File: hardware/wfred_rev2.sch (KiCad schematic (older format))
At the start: 8 parts, among them U101 L6920D

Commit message: Added Reichelt/Mouser part numbers for all parts except ESP12-E/F
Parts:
- B101: Reichelt (none) -> KEYSTONE 1013
- L101: Reichelt L-PISM 22µ -> L-242418FPS 22µ
- U101: Mouser (none) -> 511-L6920DTR
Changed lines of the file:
@@
 F 2 "myFootprints:L_2424_HandSoldering" H 4300 1400 60  0001 C CNN
 F 3 "" H 4300 1400 60  0000 C CNN
-F 4 "L-PISM 22µ" V 4300 1400 60  0001 C CNN "Reichelt"
+F 4 "L-242418FPS 22µ" V 4300 1400 60  0001 C CNN "Reichelt"
 	1    4300 1400
 	1    0    0    -1
@@
 F 3 "" H 4300 2500 60  0001 C CNN
 F 4 "L 6920 D" H 4300 2500 60  0001 C CNN "Reichelt"
+F 5 "511-L6920DTR" H 4300 2500 60  0001 C CNN "Mouser"
 	1    4300 2500
 	1    0    0    -1
@@
 F 2 "myFootprints:KEYSTONE1013" H 1200 4900 60  0001 C CNN
 F 3 "" H 1200 4900 60  0001 C CNN
+F 4 "KEYSTONE 1013" H 1200 4900 60  0001 C CNN "Reichelt"
 	1    1200 4900
 	0    1    1    0

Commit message: Created new 3D renderings
- In the process, kicad "rescued" some symbols
- Also added the value to the crystal in the schematic
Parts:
- C101, C102, C103, C104, C105: symbol C -> C-RESCUE-wfred_rev2
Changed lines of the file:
@@
 EESchema Schematic File Version 2
+LIBS:wfred_rev2-rescue
 LIBS:power
 LIBS:device
@@
 Connection ~ 5500 2200
 $Comp
-L C C101
+L C-RESCUE-wfred_rev2 C101
 U 1 1 5920B38E
 P 2150 2900
@@
 $EndComp
 $Comp
-L GND #PWR01
+L GND-RESCUE-wfred_rev2 #PWR01
 U 1 1 5920B390
 P 2150 3300
@@
 $EndComp
 $Comp
-L GND #PWR02
+L GND-RESCUE-wfred_rev2 #PWR02
 U 1 1 5920B391
 P 1850 3300
@@
 $EndComp
 $Comp
-L GND #PWR03
+L GND-RESCUE-wfred_rev2 #PWR03
 U 1 1 5920B392
 P 2450 3300
@@
 NoConn ~ 3600 2200
 $Comp
-L C C103
+L C-RESCUE-wfred_rev2 C103
 U 1 1 5920B397
 P 3300 2900
@@
 $EndComp
 $Comp
-L GND #PWR06
+L GND-RESCUE-wfred_rev2 #PWR06
 U 1 1 5920B398
 P 3300 3300
@@
 $EndComp
 $Comp
-L GND #PWR07
+L GND-RESCUE-wfred_rev2 #PWR07
 U 1 1 5920B399
 P 3500 3300
@@
 $EndComp
 $Comp
-L GND #PWR09
+L GND-RESCUE-wfred_rev2 #PWR09
 U 1 1 5920B39D
 P 6300 3300
@@
 $EndComp
 $Comp
-L GND #PWR010
+L GND-RESCUE-wfred_rev2 #PWR010
 U 1 1 5920B39E
 P 6600 3300
@@
 $EndSheet
 $Comp
-L C C102
+L C-RESCUE-wfred_rev2 C102
 U 1 1 59210DD0
 P 2450 2900
@@
 $EndComp
 $Comp
-L C C104
+L C-RESCUE-wfred_rev2 C104
 U 1 1 59210E13
 P 6300 2600
@@
 $EndComp
 $Comp
-L C C105
+L C-RESCUE-wfred_rev2 C105
 U 1 1 59210E8B
 P 6600 2600

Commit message: Switched schematic over to LiPo cell
- Removed AA battery holder
- Removed switching power regulator
- Added micro USB connector
- Added two pin battery connector
- Added LiPo charging IC
- Added 3.0V linear regulator
- Replaced ATMega328 with ATMega32
- Added F5-F8 keys
- Removed SHIFT2 key
- Moved LOCO keys from ESP to ATMega32
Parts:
- removed B101: BATT_HOLDER, myFootprints:KEYSTONE1013, symbol BATT_HOLDER
- removed C101, C102, C104: 22u/25V, Capacitors_SMD:C_0805_HandSoldering, symbol C-RESCUE-wfred_rev2
- removed C103: 100n, Capacitors_SMD:C_0805_HandSoldering, symbol C-RESCUE-wfred_rev2
- removed L101: 22u, myFootprints:L_2424_HandSoldering, symbol INDUCTOR
- removed U101: L6920D, Housings_SSOP:TSSOP-8_4.4x3mm_Pitch0.65mm, symbol L6920D
- added C101, C102: 4u7, symbol C
- added C103: 1u, symbol C
- added CON101: USB-MICRO-B, symbol USB-MINI-B
- added D101: LED - red, symbol LED
- added D102: LED - green, symbol LED
- added IC101: MCP73831T-2ACI_OT, SOT95P270X145-5N, symbol MCP73831T-2ACI_OT
- added IC102: LDL1117S30R, SOT230P700X182-4N, symbol LDL1117S30R
- added P101: BATT, symbol CONN_2
- added R101, R102: 680R, symbol R
- added R103: 2k2, symbol R
- C105: value 22u/25V -> 4u7
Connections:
- net labels added: +5V
- wire segments 26 -> 45
- no-connect marks 2 -> 3
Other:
- moved on the sheet: C105

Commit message: Changed power concept (again)
- Exchanged regulator for one with lower shutdown current
- Moved AVR directly to battery
- Added voltage regulator enable connection to AVR
- Added Speed potentiometer power supply from AVR

New power concept: AVR stays always-on (POWER DOWN MODE if not in use)
and shuts down speed potentiometer and ESP8266 when idle or battery low
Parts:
- removed IC102: LDL1117S30R, SOT230P700X182-4N, symbol LDL1117S30R
- added IC102: NCV8161BSN300T1G, SOT95P275X110-5N, symbol NCV8161BSN300T1G
- C105: value 4u7 -> 1u
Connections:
- net labels added: ESP_ENABLE
- wire segments 45 -> 47
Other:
- moved on the sheet: C105

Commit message: First PCB draft for LiPo version
- Returned to ATMega328 / not enough space for ATMega32
- Moved to multiplexing key and direction inputs -> kept F5-F8
- Most traces are now 0.5mm wide
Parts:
- C101, C102, C103, R101, R102, R103: footprint (none) -> Capacitors_SMD:C_0805_HandSoldering
- CON101: footprint (none) -> Connectors_USB:USB_Micro-B_Molex-105017-0001; Mouser (none) -> 538-105017-0001
- D101, D102: footprint (none) -> myFootprints:LED_D3.0mm
- IC101: footprint SOT95P270X145-5N -> MCP73831T-2ACI_OT:SOT95P270X145-5N
- IC102: footprint SOT95P275X110-5N -> NCV8161BSN300T1G:SOT95P275X110-5N
- P101: footprint (none) -> Pin_Headers:Pin_Header_Angled_1x02_Pitch2.54mm
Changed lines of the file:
@@
 F 0 "P101" V 1350 1600 40  0000 C CNN
 F 1 "BATT" V 1450 1600 40  0000 C CNN
-F 2 "" H 1400 1600 60  0001 C CNN
+F 2 "Pin_Headers:Pin_Header_Angled_1x02_Pitch2.54mm" H 1400 1600 60  0001 C CNN
 F 3 "" H 1400 1600 60  0001 C CNN
 	1    1400 1600
@@
 F 0 "CON101" H 1800 3950 60  0000 C CNN
 F 1 "USB-MICRO-B" H 2000 3000 60  0000 C CNN
-F 2 "" H 2050 3500 60  0001 C CNN
+F 2 "Connectors_USB:USB_Micro-B_Molex-105017-0001" H 2050 3500 60  0001 C CNN
 F 3 "" H 2050 3500 60  0001 C CNN
+F 4 "538-105017-0001" H 2050 3500 60  0001 C CNN "Mouser"
 	1    2050 3500
 	1    0    0    -1
@@
 F 0 "C101" H 4200 3300 40  0000 L CNN
 F 1 "4u7" H 4206 3115 40  0000 L CNN
-F 2 "" H 4238 3050 30  0000 C CNN
+F 2 "Capacitors_SMD:C_0805_HandSoldering" H 4238 3050 30  0001 C CNN
 F 3 "" H 4200 3200 60  0000 C CNN
 	1    4200 3200
@@
 F 0 "R101" V 3780 1550 40  0000 C CNN
 F 1 "680R" V 3707 1551 40  0000 C CNN
-F 2 "" V 3630 1550 30  0000 C CNN
+F 2 "Capacitors_SMD:C_0805_HandSoldering" V 3630 1550 30  0001 C CNN
 F 3 "" H 3700 1550 30  0000 C CNN
 	1    3700 1550
@@
 F 0 "R102" V 3780 3250 40  0000 C CNN
 F 1 "680R" V 3707 3251 40  0000 C CNN
-F 2 "" V 3630 3250 30  0000 C CNN
+F 2 "Capacitors_SMD:C_0805_HandSoldering" V 3630 3250 30  0001 C CNN
 F 3 "" H 3700 3250 30  0000 C CNN
 	1    3700 3250
@@
 F 0 "D101" H 3700 2200 50  0000 C CNN
 F 1 "LED - red" H 3700 2000 50  0000 C CNN
-F 2 "" H 3700 2100 60  0000 C CNN
+F 2 "myFootprints:LED_D3.0mm" H 3700 2100 60  0001 C CNN
 F 3 "" H 3700 2100 60  0000 C CNN
 	1    3700 2100
@@
 F 0 "D102" H 3700 2800 50  0000 C CNN
 F 1 "LED - green" H 3700 2600 50  0000 C CNN
-F 2 "" H 3700 2700 60  0000 C CNN
+F 2 "myFootprints:LED_D3.0mm" H 3700 2700 60  0001 C CNN
 F 3 "" H 3700 2700 60  0000 C CNN
 	1    3700 2700
@@
 F 0 "C102" H 6400 3300 40  0000 L CNN
 F 1 "4u7" H 6406 3115 40  0000 L CNN
-F 2 "" H 6438 3050 30  0000 C CNN
+F 2 "Capacitors_SMD:C_0805_HandSoldering" H 6438 3050 30  0001 C CNN
 F 3 "" H 6400 3200 60  0000 C CNN
 	1    6400 3200
@@
 F 0 "R103" V 6180 3250 40  0000 C CNN
 F 1 "2k2" V 6107 3251 40  0000 C CNN
-F 2 "" V 6030 3250 30  0000 C CNN
+F 2 "Capacitors_SMD:C_0805_HandSoldering" V 6030 3250 30  0001 C CNN
 F 3 "" H 6100 3250 30  0000 C CNN
 	1    6100 3250
@@
 F 0 "C103" H 7500 2600 40  0000 L CNN
 F 1 "1u" H 7506 2415 40  0000 L CNN
-F 2 "" H 7538 2350 30  0000 C CNN
+F 2 "Capacitors_SMD:C_0805_HandSoldering" H 7538 2350 30  0001 C CNN
 F 3 "" H 7500 2500 60  0000 C CNN
 	1    7500 2500
@@
 F 0 "IC101" H 5850 2700 50  0000 L CNN
 F 1 "MCP73831T-2ACI_OT" H 5850 2600 50  0000 L CNN
-F 2 "SOT95P270X145-5N" H 5850 2500 50  0001 L CNN
+F 2 "MCP73831T-2ACI_OT:SOT95P270X145-5N" H 5850 2500 50  0001 L CNN
 F 3 "http://ww1.microchip.com/downloads/en/DeviceDoc/20001984g.pdf" H 5850 2400 50  0001 L CNN
 F 4 "Li-Ion Charge Controller 4.2V SOT23-5" H 5850 2300 50  0001 L CNN "Description"
@@
 F 0 "IC102" H 9550 2700 50  0000 L CNN
 F 1 "NCV8161BSN300T1G" H 9550 2600 50  0000 L CNN
-F 2 "SOT95P275X110-5N" H 9550 2500 50  0001 L CNN
+F 2 "NCV8161BSN300T1G:SOT95P275X110-5N" H 9550 2500 50  0001 L CNN
 F 3 "http://www.onsemi.com/pub/Collateral/NCV8161-D.PDF" H 9550 2400 50  0001 L CNN
 F 4 "450 mA, Ultra-Low Noise and High PSRR LDO Regulator for RF and Analog Circuits 3.0V, Non-Active Discharge, TSOP-5" H 9550 2300 50  0001 L CNN "Description"

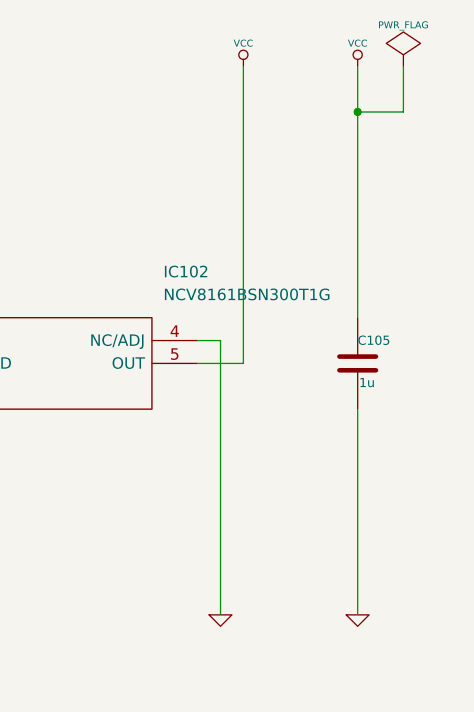
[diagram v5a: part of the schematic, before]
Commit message: Added R104 - discharging resistor on 3V line...
...this reduces the time until the ESP12 can be reactivated because its
supply voltage drops much quicker with this resistor installed.

Increases active current by approx 0.3mA (3V / 10kOhm)
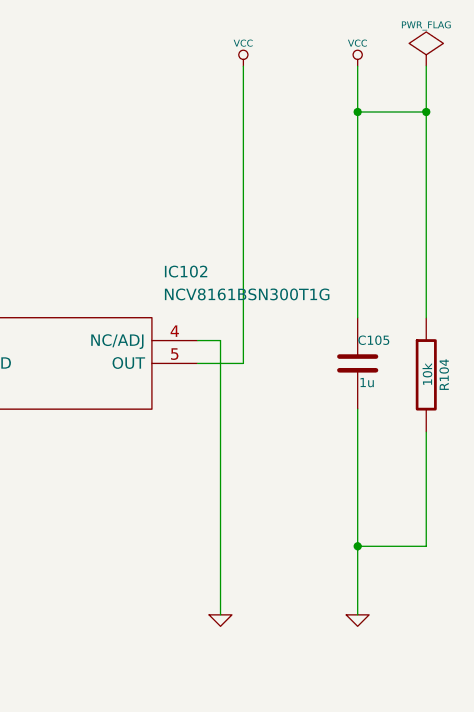
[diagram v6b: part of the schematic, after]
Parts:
- added R104: 10k, Capacitors_SMD:C_0805_HandSoldering, symbol R
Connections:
- net GND: now also R104.2
- net VCC: now also R104.1
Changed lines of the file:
@@
 L PWR_FLAG #FLG021
 U 1 1 5BDFDCEB
-P 10600 1200
-F 0 "#FLG021" H 10600 1295 30  0001 C CNN
-F 1 "PWR_FLAG" H 10600 1380 30  0000 C CNN
-F 2 "" H 10600 1200 60  0001 C CNN
-F 3 "" H 10600 1200 60  0001 C CNN
-	1    10600 1200
+P 10700 1200
+F 0 "#FLG021" H 10700 1295 30  0001 C CNN
+F 1 "PWR_FLAG" H 10700 1380 30  0000 C CNN
+F 2 "" H 10700 1200 60  0001 C CNN
+F 3 "" H 10700 1200 60  0001 C CNN
+	1    10700 1200
 	1    0    0    -1
 $EndComp
 Wire Wire Line
-	10600 1200 10600 1400
+	10700 1200 10700 2300
 Wire Wire Line
-	10600 1400 10400 1400
+	10700 1400 10400 1400
 Connection ~ 10400 1400
 $Comp
@@
 Wire Wire Line
 	8300 2600 8500 2600
+$Comp
+L R R104
+U 1 1 5CD0A628
+P 10700 2550
+F 0 "R104" V 10780 2550 40  0000 C CNN
+F 1 "10k" V 10707 2551 40  0000 C CNN
+F 2 "Capacitors_SMD:C_0805_HandSoldering" V 10630 2550 30  0001 C CNN
+F 3 "" H 10700 2550 30  0000 C CNN
+	1    10700 2550
+	1    0    0    -1
+$EndComp
+Connection ~ 10700 1400
+Wire Wire Line
+	10700 2800 10700 3300
+Wire Wire Line
+	10700 3300 10400 3300
+Connection ~ 10400 3300
 $EndSCHEMATC

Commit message: Exchanged 3mm white LEDs for 5mm white LEDs...
...with specific type

Also updated supplier fields for a few parts
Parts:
- C103: Reichelt (none) -> X7R-G0805 1,0/25
- C105: Reichelt X5R-G0805 22/25 -> X7R-G0805 1,0/25
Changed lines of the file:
@@
 F 2 "Capacitors_SMD:C_0805_HandSoldering" H 7538 2350 30  0001 C CNN
 F 3 "" H 7500 2500 60  0000 C CNN
+F 4 "X7R-G0805 1,0/25" H 7500 2500 60  0001 C CNN "Reichelt"
 	1    7500 2500
 	1    0    0    -1
@@
 F 2 "Capacitors_SMD:C_0805_HandSoldering" H 10438 2350 30  0001 C CNN
 F 3 "" H 10400 2500 60  0000 C CNN
-F 4 "X5R-G0805 22/25" H 10400 2500 60  0001 C CNN "Reichelt"
+F 4 "X7R-G0805 1,0/25" H 10400 2500 60  0001 C CNN "Reichelt"
 	1    10400 2500
 	1    0    0    -1

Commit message: Updated schematic and PCB for kicad 5.1.4
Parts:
- C101, C102, C103: symbol C -> device:C
- C105: symbol C-RESCUE-wfred_rev2 -> wfred_rev2-rescue:C-RESCUE-wfred_rev2
- CON101: symbol USB-MINI-B -> conn:USB-MINI-B
- D101, D102: symbol LED -> device:LED
- IC101: symbol MCP73831T-2ACI_OT -> MCP73831T-2ACI_OT:MCP73831T-2ACI_OT
- IC102: symbol NCV8161BSN300T1G -> NCV8161BSN300T1G:NCV8161BSN300T1G
- P101: symbol CONN_2 -> conn:CONN_2
- R101, R102, R103, R104: symbol R -> device:R
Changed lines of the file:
@@
-EESchema Schematic File Version 2
-LIBS:wfred_rev2-rescue
-LIBS:power
-LIBS:device
-LIBS:transistors
-LIBS:conn
-LIBS:linear
-LIBS:regul
-LIBS:74xx
-LIBS:cmos4000
-LIBS:adc-dac
-LIBS:memory
-LIBS:xilinx
-LIBS:microcontrollers
-LIBS:dsp
-LIBS:microchip
-LIBS:analog_switches
-LIBS:motorola
-LIBS:texas
-LIBS:intel
-LIBS:audio
-LIBS:interface
-LIBS:digital-audio
-LIBS:philips
-LIBS:display
-LIBS:cypress
-LIBS:siliconi
-LIBS:opto
-LIBS:atmel
-LIBS:contrib
-LIBS:valves
-LIBS:my_devices
-LIBS:ESP8266
-LIBS:LDL1117S30R
-LIBS:MCP73831T-2ACI_OT
-LIBS:NCV8161BSN300T1G
+EESchema Schematic File Version 4
 LIBS:wfred_rev2-cache
-EELAYER 25 0
+EELAYER 30 0
 EELAYER END
 $Descr A4 11693 8268
@@
 $EndDescr
 Wire Wire Line
-	10400 1200 10400 2300
-Wire Wire Line
-	10400 2700 10400 3600
-$Comp
-L GND-RESCUE-wfred_rev2 #PWR01
+	10400 1200 10400 1400
+Wire Wire Line
+	10400 2700 10400 3300
+$Comp
+L wfred_rev2-rescue:GND-RESCUE-wfred_rev2 #PWR01
 U 1 1 5920B391
 P 2200 2200
@@
 $EndComp
 $Comp
-L +BATT #PWR02
+L power:+BATT #PWR02
 U 1 1 5920B394
 P 2800 1250
@@
 $EndComp
 $Comp
-L GND-RESCUE-wfred_rev2 #PWR03
+L wfred_rev2-rescue:GND-RESCUE-wfred_rev2 #PWR03
 U 1 1 5920B39E
 P 10400 3600
@@
 $EndSheet
 $Comp
-L PWR_FLAG #FLG04
+L power:PWR_FLAG #FLG04
 U 1 1 59214BB2
 P 2200 1250
@@
 $EndSheet
 $Comp
-L CONN_2 P101
+L conn:CONN_2 P101
 U 1 1 5BDF535A
 P 1400 1600
@@
 Connection ~ 2200 1700
 Wire Wire Line
-	2200 1250 2200 2200
-Wire Wire Line
-	1750 1500 3000 1500
-$Comp
-L USB-MINI-B CON101
+	2200 1250 2200 1700
+Wire Wire Line
+	1750 1500 2800 1500
+$Comp
+L conn:USB-MINI-B CON101
 U 1 1 5BDF5403
 P 2050 3500
@@
 $EndComp
 $Comp
-L GND #PWR05
+L power:GND #PWR05
 U 1 1 5BDF5538
 P 2800 4200
@@
 	2600 3200 2800 3200
 Wire Wire Line
-	2800 3200 2800 4200
+	2800 3200 2800 3350
 Wire Wire Line
 	2600 3350 2800 3350
@@
 Connection ~ 2800 3800
 $Comp
-L GND #PWR06
+L power:GND #PWR06
 U 1 1 5BDF55B7
 P 1300 4200
@@
 NoConn ~ 1500 3650
 $Comp
-L VCC #PWR07
+L power:VCC #PWR07
 U 1 1 5BDF5646
 P 10400 1200
@@
 $EndComp
 $Comp
-L +5V #PWR08
+L power:+5V #PWR08
 U 1 1 5BDF5666
 P 1300 2950
@@
 	1300 2950 1300 3200
 Wire Wire Line
-	1100 3200 1500 3200
-$Comp
-L +BATT #PWR09
+	1100 3200 1300 3200
+$Comp
+L power:+BATT #PWR09
 U 1 1 5BDF64A0
 P 4200 1200
@@
 $EndComp
 Wire Wire Line
-	4200 1200 4200 3000
-$Comp
-L C C101
+	4200 1200 4200 2600
+$Comp
+L device:C C101
 U 1 1 5BDF64E4
 P 4200 3200
@@
 Connection ~ 4200 2600
 $Comp
-L GND #PWR010
+L power:GND #PWR010
 U 1 1 5BDF6575
 P 4200 3600
@@
 	4200 3600 4200 3400
 $Comp
-L GND #PWR011
+L power:GND #PWR011
 U 1 1 5BDF65B7
 P 4500 3600
@@
 	4500 2500 4900 2500
 $Comp
-L R R101
+L device:R R101
 U 1 1 5BDF69E9
 P 3700 1550
@@
 $EndComp
 $Comp
-L R R102
+L device:R R102
 U 1 1 5BDF6A99
 P 3700 3250
@@
 $EndComp
 $Comp
-L LED D101
+L device:LED D101
 U 1 1 5BDF6C34
 P 3700 2100
@@
 $EndComp
 $Comp
-L LED D102
+L device:LED D102
 U 1 1 5BDF6CF2
 P 3700 2700
@@
 	4900 2400 3700 2400
 Wire Wire Line
-	3700 2300 3700 2500
+	3700 2300 3700 2400
 Connection ~ 3700 2400
 Wire Wire Line
@@
 	3700 2900 3700 3000
 $Comp
-L GND #PWR012
+L power:GND #PWR012
 U 1 1 5BDF6E99
 P 3700 3600
@@
 	3700 3500 3700 3600
 $Comp
-L +5V #PWR013
+L power:+5V #PWR013
 U 1 1 5BDF6FC9
 P 3700 1200
@@
 	3700 1200 3700 1300
 $Comp
-L C C102
+L device:C C102
 U 1 1 5BDF745F
 P 6400 3200
@@
 $EndComp
 $Comp
-L GND #PWR014
+L power:GND #PWR014
 U 1 1 5BDF761A
 P 6400 3600
@@
 	6000 2400 6400 2400
 Wire Wire Line
-	6400 1200 6400 3000
+	6400 1200 6400 2400
 Connection ~ 6400 2400
 $Comp
-L +5V #PWR015
+L power:+5V #PWR015
 U 1 1 5BDF76F6
 P 6400 1200
@@
 $EndComp
 $Comp
-L R R103
+L device:R R103
 U 1 1 5BDF77A8
 P 6100 3250
@@
 	6100 2500 6100 3000
 $Comp
-L GND #PWR016
+L power:GND #PWR016
 U 1 1 5BDF79BD
 P 6100 3600
@@
 	6100 3500 6100 3600
 $Comp
-L C C103
+L device:C C103
 U 1 1 5BDF7FBD
 P 7500 2500
@@
 $EndComp
 $Comp
-L +BATT #PWR017
+L power:+BATT #PWR017
 U 1 1 5BDF800C
 P 7500 1200
@@
 	7500 1200 7500 2300
 $Comp
-L GND #PWR018
+L power:GND #PWR018
 U 1 1 5BDF8082
 P 7500 3600
@@
 	2800 1500 2800 1250
 $Comp
-L C-RESCUE-wfred_rev2 C105
+L wfred_rev2-rescue:C-RESCUE-wfred_rev2 C105
 U 1 1 59210E8B
 P 10400 2500
@@
 $EndComp
 $Comp
-L PWR_FLAG #FLG019
+L power:PWR_FLAG #FLG019
 U 1 1 5BDFC97D
 P 1100 2900
@@
 Connection ~ 1300 3200
 $Comp
-L PWR_FLAG #FLG020
+L power:PWR_FLAG #FLG020
 U 1 1 5BDFCAA6
 P 3000 1200
@@
 Connection ~ 2800 1500
 $Comp
-L PWR_FLAG #FLG021
+L power:PWR_FLAG #FLG021
 U 1 1 5BDFDCEB
 P 10700 1200
@@
 $EndComp
 Wire Wire Line
-	10700 1200 10700 2300
+	10700 1200 10700 1400
 Wire Wire Line
 	10700 1400 10400 1400
 Connection ~ 10400 1400
 $Comp
-L MCP73831T-2ACI_OT IC101
+L MCP73831T-2ACI_OT:MCP73831T-2ACI_OT IC101
 U 1 1 5BDF6387
 P 4900 2400
@@
 $EndComp
 $Comp
-L NCV8161BSN300T1G IC102
+L NCV8161BSN300T1G:NCV8161BSN300T1G IC102
 U 1 1 5BE0A471
 P 8500 2400
@@
 $EndComp
 $Comp
-L GND #PWR022
+L power:GND #PWR022
 U 1 1 5BE0A873
 P 8400 3600
@@
 	8400 2500 8500 2500
 $Comp
-L +BATT #PWR023
+L power:+BATT #PWR023
 U 1 1 5BE0A8E4
 P 8400 1200
@@
 	9800 2400 9800 3600
 $Comp
-L GND #PWR024
+L power:GND #PWR024
 U 1 1 5BE0A9A9
 P 9800 3600
@@
 $EndComp
 $Comp
-L VCC #PWR025
+L power:VCC #PWR025
 U 1 1 5BE0AA4D
 P 9900 1200
@@
 	8300 2600 8500 2600
 $Comp
-L R R104
+L device:R R104
 U 1 1 5CD0A628
 P 10700 2550
@@
 	10700 3300 10400 3300
 Connection ~ 10400 3300
+Wire Wire Line
+	2200 1700 2200 2200
+Wire Wire Line
+	2800 3350 2800 3650
+Wire Wire Line
+	2800 3650 2800 3800
+Wire Wire Line
+	2800 3800 2800 4200
+Wire Wire Line
+	4200 2600 4200 3000
+Wire Wire Line
+	3700 2400 3700 2500
+Wire Wire Line
+	6400 2400 6400 3000
+Wire Wire Line
+	1300 3200 1500 3200
+Wire Wire Line
+	2800 1500 3000 1500
+Wire Wire Line
+	10400 1400 10400 2300
+Wire Wire Line
+	10700 1400 10700 2300
+Wire Wire Line
+	10400 3300 10400 3600
 $EndSCHEMATC
